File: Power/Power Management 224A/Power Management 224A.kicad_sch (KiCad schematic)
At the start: 18 parts, among them J1 USB_C_Receptacle_USB2.0_16P, Q1 2N7002, SW1 SW_DIP_x03, U1 AMS1117-3.3

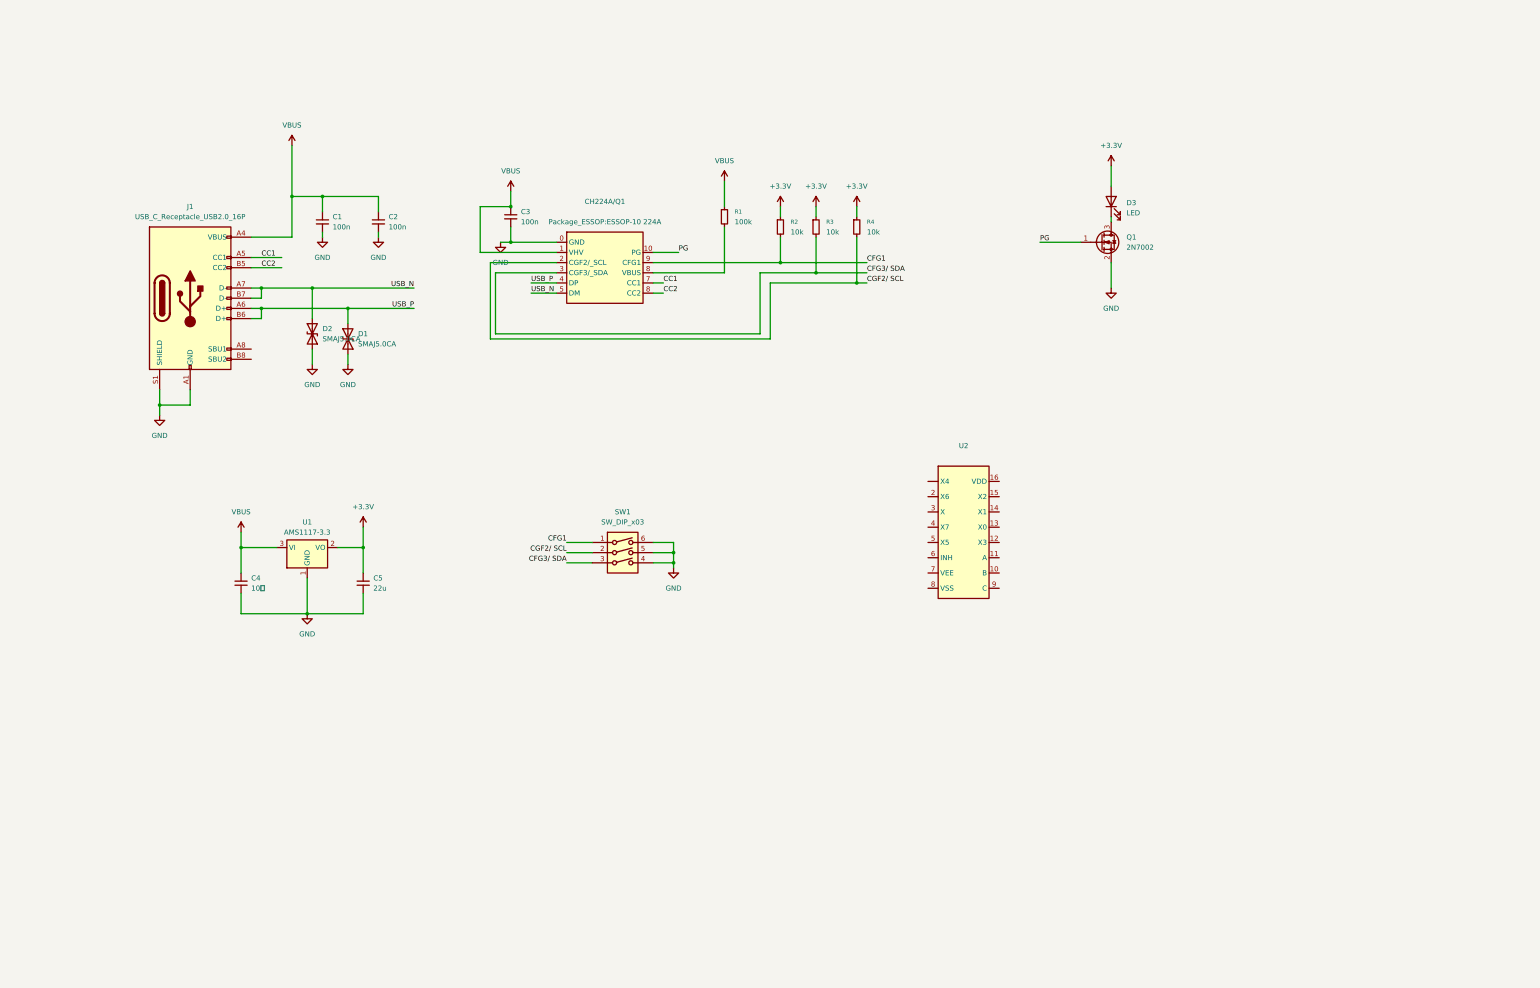
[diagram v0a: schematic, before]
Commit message: New USB-Power 5V-28V
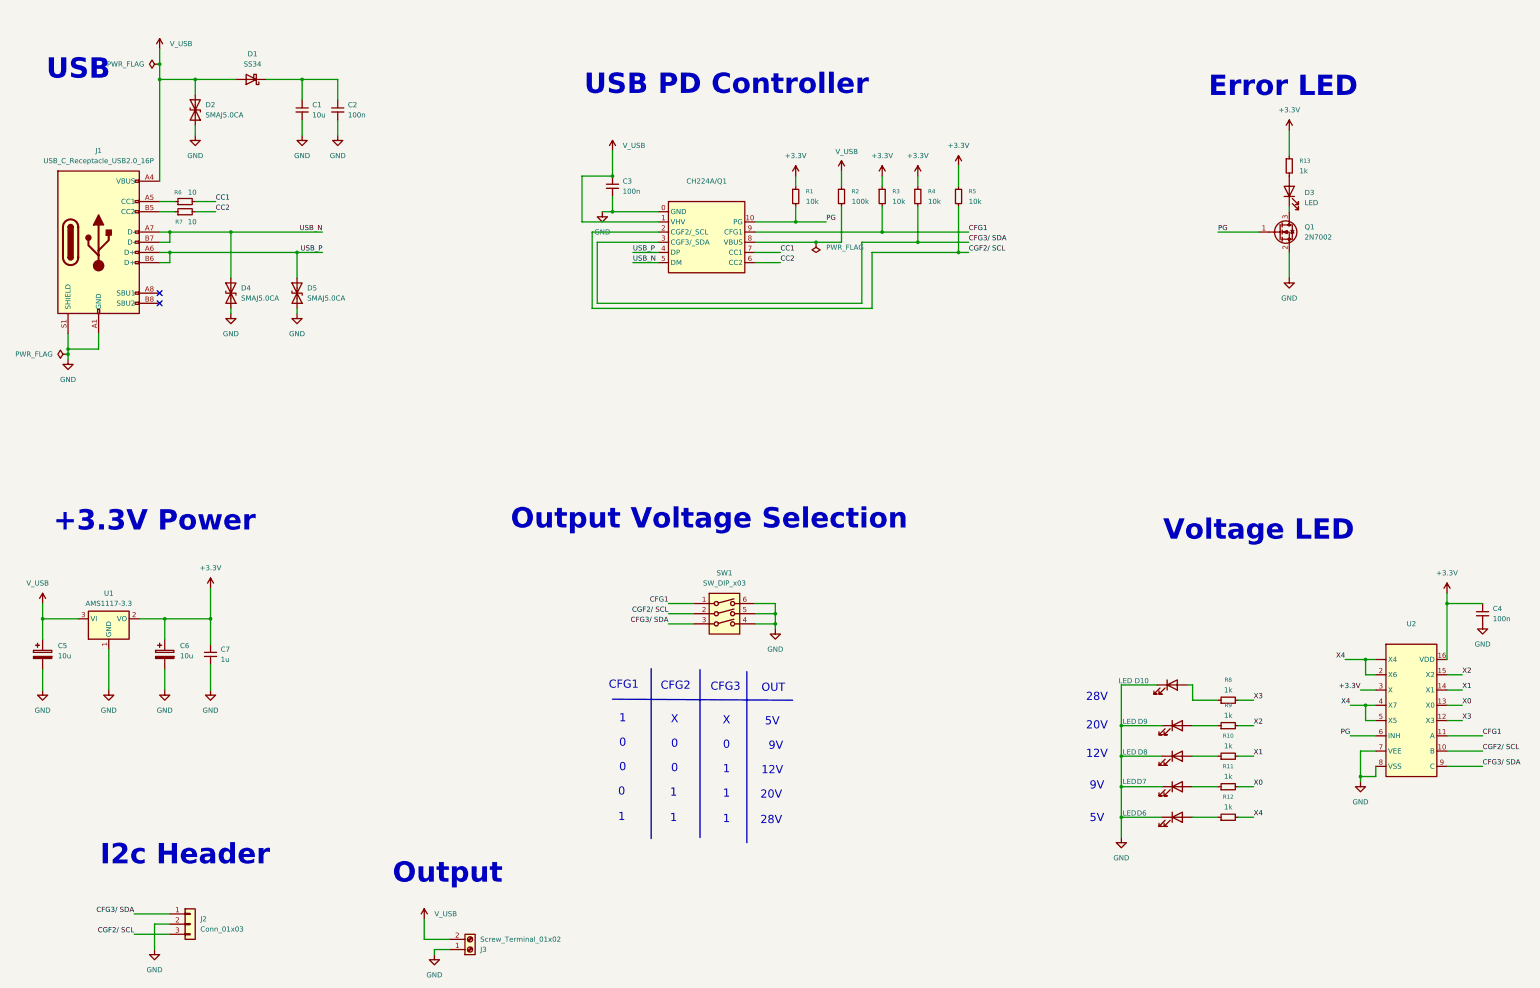
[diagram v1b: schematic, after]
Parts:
- removed C5: 22u, symbol Device:C_Small
- removed D1: SMAJ5.0CA, Diode_SMD:D_SOD-123, symbol Diode:SMAJ5.0CA
- added C5, C6: 10u, Capacitor_SMD:CP_Elec_3x5.4, symbol Device:C_Polarized
- added C7: 1u, Capacitor_SMD:C_0603_1608Metric_Pad1.08x0.95mm_HandSolder, symbol Device:C_Small
- added D1: SS34, Diode_SMD:D_SMA, symbol Diode:SS34
- added D10, D6, D7, D8, D9: LED, LED_SMD:LED_0805_2012Metric_Pad1.15x1.40mm_HandSolder, symbol Device:LED
- added D4, D5: SMAJ5.0CA, Diode_SMD:D_SOD-123, symbol Diode:SMAJ5.0CA
- added J2: Conn_01x03, Connector_PinHeader_2.54mm:PinHeader_1x03_P2.54mm_Vertical, symbol Connector_Generic:Conn_01x03
- added J3: Screw_Terminal_01x02, TerminalBlock_Phoenix:TerminalBlock_Phoenix_MKDS-1,5-2_1x02_P5.00mm_Horizontal, symbol Connector:Screw_Terminal_01x02
- added R1: 10k, Resistor_SMD:R_0603_1608Metric_Pad0.98x0.95mm_HandSolder, symbol Device:R_Small
- added R10, R11, R12, R13, R8, R9: 1k, Resistor_SMD:R_0603_1608Metric_Pad0.98x0.95mm_HandSolder, symbol Device:R_Small
- added R6, R7: 10, Resistor_SMD:R_0603_1608Metric_Pad0.98x0.95mm_HandSolder, symbol Device:R_Small
- C1: value 100n -> 10u; footprint (none) -> Capacitor_SMD:C_1206_3216Metric_Pad1.33x1.80mm_HandSolder
- C2, C3: footprint (none) -> Capacitor_SMD:C_0603_1608Metric_Pad1.08x0.95mm_HandSolder
- C4: value 10ี -> 100n; footprint 10u -> Capacitor_SMD:C_0603_1608Metric_Pad1.08x0.95mm_HandSolder
- D3: footprint (none) -> LED_SMD:LED_0805_2012Metric_Pad1.15x1.40mm_HandSolder
- R2: renamed from R1; footprint (none) -> Resistor_SMD:R_0603_1608Metric_Pad0.98x0.95mm_HandSolder
- R3: renamed from R2; footprint (none) -> Resistor_SMD:R_0603_1608Metric_Pad0.98x0.95mm_HandSolder
- R4: renamed from R3; footprint (none) -> Resistor_SMD:R_0603_1608Metric_Pad0.98x0.95mm_HandSolder
- R5: renamed from R4; footprint (none) -> Resistor_SMD:R_0603_1608Metric_Pad0.98x0.95mm_HandSolder
- SW1: footprint (none) -> Button_Switch_SMD:SW_DIP_SPSTx03_Slide_6.7x9.18mm_W6.73mm_P2.54mm_LowProfile_JPin
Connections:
- net +3.3V: now also C4.1, U2.16 (VDD), U2.3 (X), C6.1, C7.1, R1.1, R13.1; no longer D3.2 (A)
- net CC1: now also R6.2; no longer J1.A5 (CC1)
- net CC2: now also CH224A/Q1.6 (CC2), R7.2; no longer CH224A/Q1.8 (CC2), J1.B5 (CC2)
- net CFG1: now also U2.11 (A)
- net CFG3/ SDA: now also U2.9 (C), J2.1 (Pin_1)
- net CGF2/ SCL: now also U2.10 (B), J2.3 (Pin_3)
- net GND: now also U2.7 (VEE), U2.8 (VSS), C5.2, C6.2, C7.2, D10.1 (K), D4.1 (A1), D5.1 (A1), D6.1 (K), D7.1 (K), D8.1 (K), D9.1 (K), J2.2 (Pin_2), J3.1 (Pin_1)
- net PG: now also U2.6 (INH), R1.2
- net USB_N: now also D4.2 (A2); no longer D2.2 (A2)
- net USB_P: now also D5.2 (A2)
- net X4: now reaches U2. (X4)
- net X4: now also U2.2 (X6), U2.4 (X7), U2.5 (X5), R12.2
- net X3: now reaches U2.12 (X3)
- net X3: now also R8.2
- net X0: now reaches U2.13 (X0)
- net X0: now also R11.2
- net X1: now reaches U2.14 (X1)
- net X1: now also R10.2
- net X2: now reaches U2.15 (X2)
- net X2: now also R9.2
- net VBUS renamed V_USB
- net V_USB: now also D2.2 (A2), C5.1, D1.2 (A), J3.2 (Pin_2); no longer C1.1, C2.1, C4.1
- new net: D9.2 (A), R9.1
- new net: C1.1, C2.1, D1.1 (K)
- new net: J1.A5 (CC1), R6.1
- new net: J1.B5 (CC2), R7.1
- new net: D3.2 (A), R13.2
- new net: D7.2 (A), R11.1
- new net: D6.2 (A), R12.1
- new net: D10.2 (A), R8.1
- new net: D8.2 (A), R10.1
- no-connect marks 0 -> 2
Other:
- note added: "+3.3V Power"
- note added: "0"
- note added: "1"
- note added: "12V"
- note added: "20V"
- note added: "28V"
- note added: "5V"
- note added: "9V"
- note added: "CFG1"
- note added: "CFG2"
- note added: "CFG3"
- note added: "Error LED"
- note added: "I2c Header"
- note added: "OUT"
- note added: "Output"
- note added: "Output Voltage Selection"
- note added: "USB"
- note added: "USB PD Controller"
- note added: "Voltage LED"
- note added: "X"
- moved on the sheet: C1, C2, C3, D2, D3, J1, Q1, R2, R3, R4, R5, SW1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

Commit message: Update Viapad
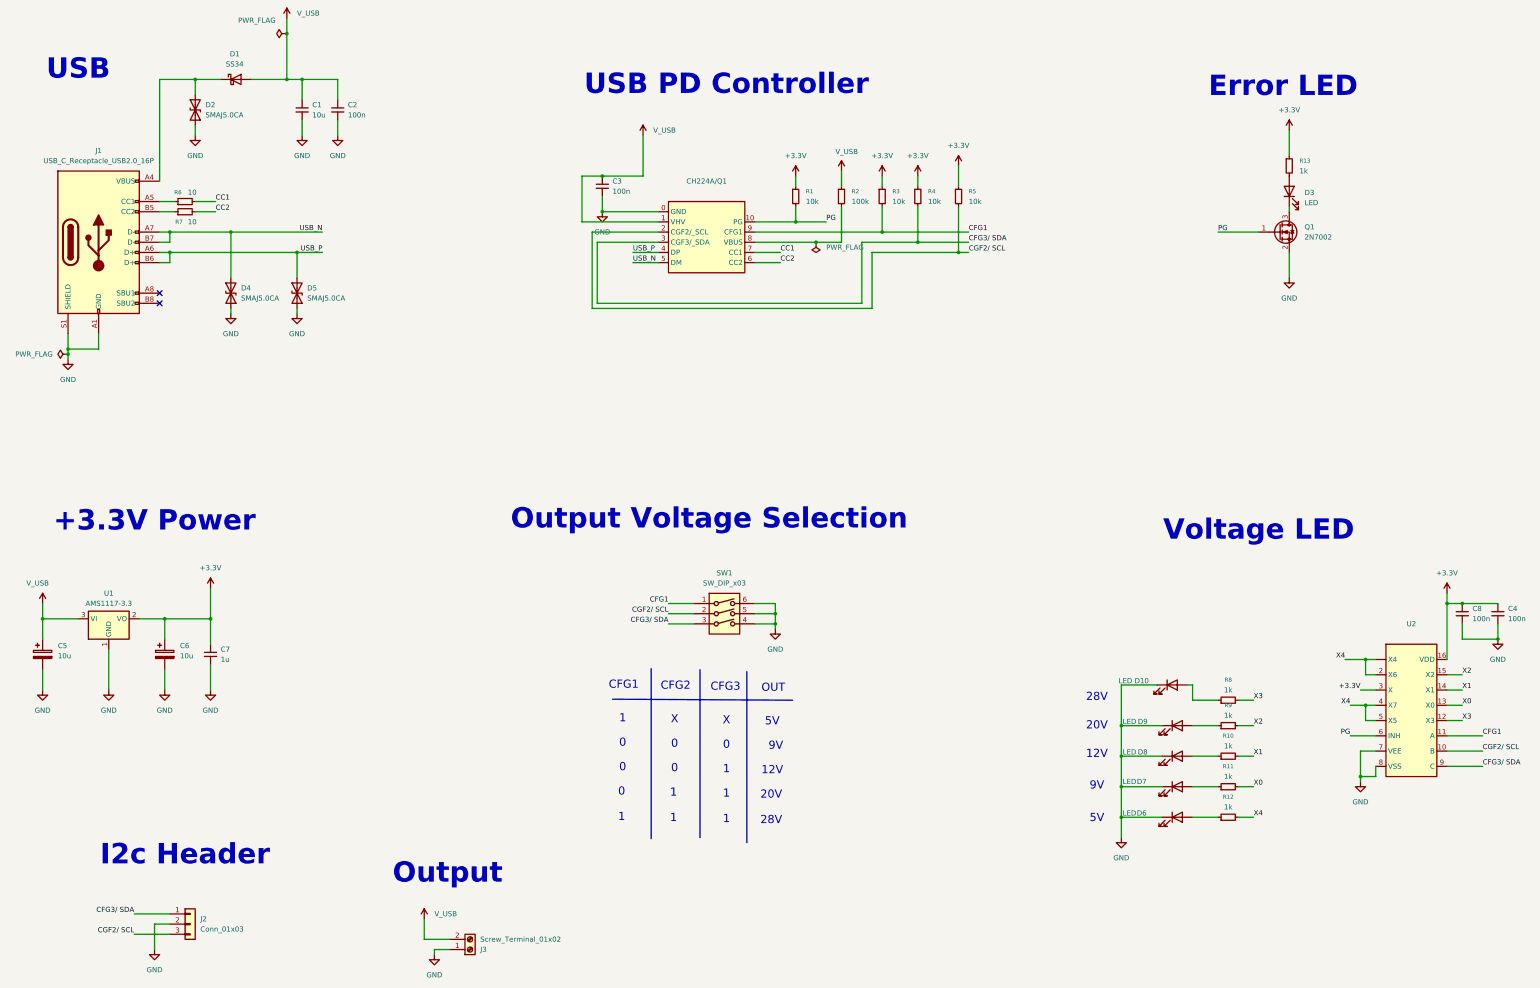
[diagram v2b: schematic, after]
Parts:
- added C8: 100n, Capacitor_SMD:C_0603_1608Metric_Pad1.08x0.95mm_HandSolder, symbol Device:C_Small
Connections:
- net +3.3V: now also C8.1
- net GND: now also C8.2
- net V_USB: now also C1.1, C2.1; no longer D2.2 (A2), J1.A4 (VBUS), J1.A9 (VBUS), J1.B4 (VBUS), J1.B9 (VBUS)
- new net: D1.1 (K), D2.2 (A2), J1.A4 (VBUS), J1.A9 (VBUS), J1.B4 (VBUS), J1.B9 (VBUS)
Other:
- moved on the sheet: C3, C4, D1
